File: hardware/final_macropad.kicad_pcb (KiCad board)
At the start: 4 copper layers, 91.2 x 120.5 mm, 69 parts, among them J2 2137160001, SW1 SKQGADE010, U1 ATmega32U4-A, U2 USBLC6-2SC6, U3 DM-OLED096-636, Y1 16MHz

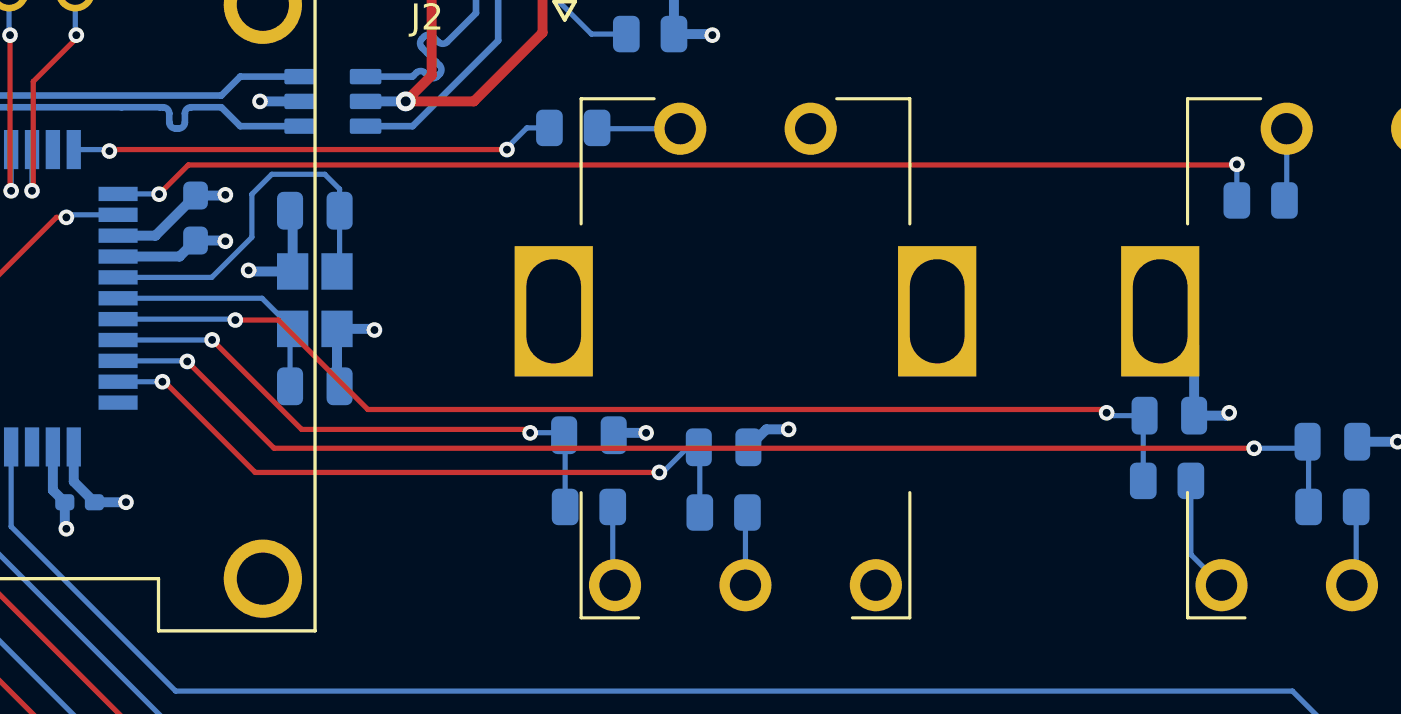
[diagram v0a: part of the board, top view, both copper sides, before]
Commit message: move trace away from through-hole
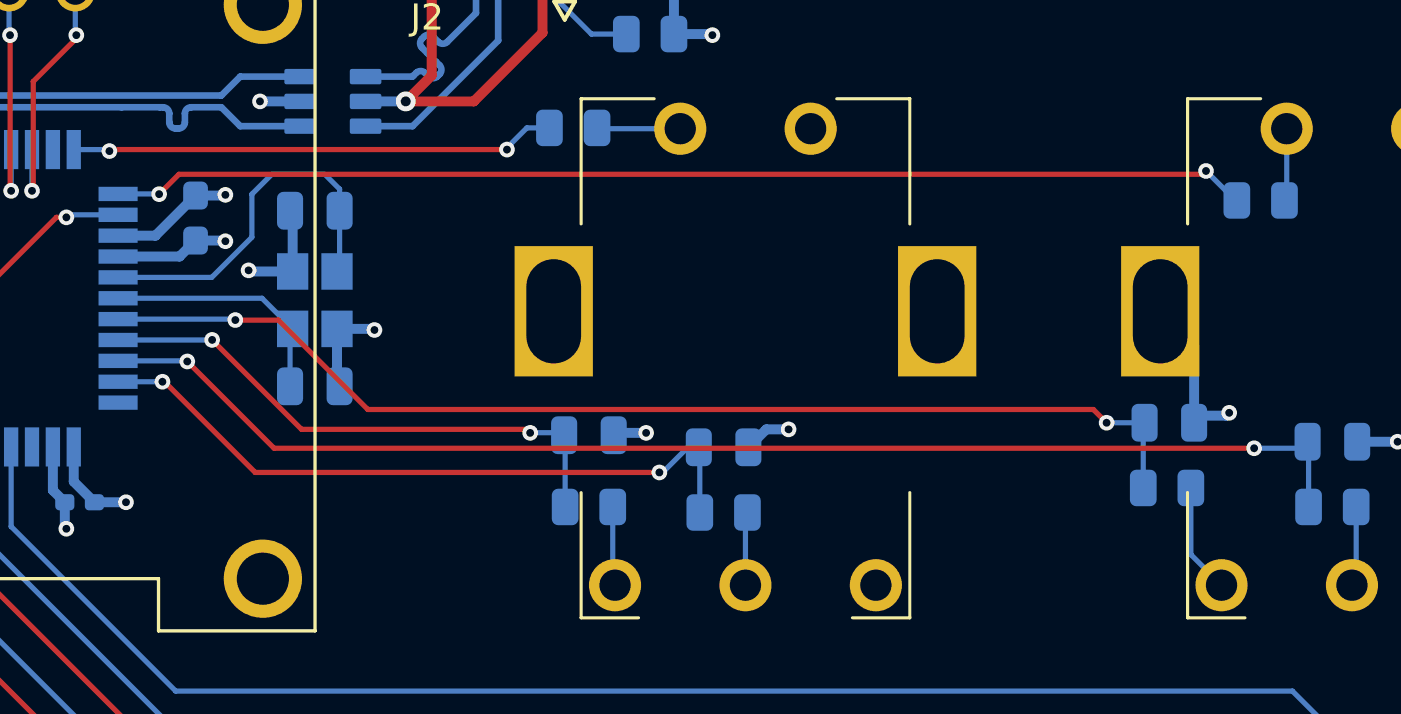
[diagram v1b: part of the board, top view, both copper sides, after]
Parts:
- moved C8 0.27 mm to (95.8, 49.0)
- moved R5 0.27 mm to (95.7, 51.5)
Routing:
- net SW0: track 44.7 -> 43.7 mm
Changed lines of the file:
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@@
 	(footprint "Resistor_SMD:R_0805_2012Metric"
 		(layer "B.Cu")
-		(at 95.6625 51.25)
+		(at 95.6625 51.522)
 		(descr "Resistor SMD 0805 (2012 Metric), square (rectangular) end terminal, IPC-7351 nominal, (Body size source: IPC-SM-782 page 72, https://www.pcb-3d.com/wordpress/wp-content/uploads/ipc-sm-782a_amendment_1_and_2.pdf), generated with kicad-footprint-generator")
 		(tags "resistor")
@@
 	(footprint "Capacitor_SMD:C_0805_2012Metric"
 		(layer "B.Cu")
-		(at 95.75 48.75)
+		(at 95.75 49.022)
 		(descr "Capacitor SMD 0805 (2012 Metric), square (rectangular) end terminal, IPC-7351 nominal, (Body size source: IPC-SM-782 page 76, https://www.pcb-3d.com/wordpress/wp-content/uploads/ipc-sm-782a_amendment_1_and_2.pdf, https://docs.google.com/spreadsheets/d/1BsfQQcO9C6DZCsRaXUlFlo91Tg2WpOkGARC1WS5S8t0/edit?usp=sharing), generated with kicad-footprint-generator")
 		(tags "capacitor")
@@
 	(segment
 		(start 97.935 48.75)
-		(end 98.044 48.641)
+		(end 96.7 48.75)
 		(width 0.381)
 		(layer "B.Cu")
@@
 	)
 	(segment
+		(start 96.7 46.05)
+		(end 95.4 44.75)
+		(width 0.381)
+		(layer "B.Cu")
+		(net 8)
+	)
+	(segment
 		(start 63.842 47.525)
 		(end 63.942 47.625)
@@
 	)
 	(segment
+		(start 96.7 48.75)
+		(end 96.7 46.05)
+		(width 0.381)
+		(layer "B.Cu")
+		(net 8)
+	)
+	(segment
 		(start 65.235 45.423)
 		(end 65.278 45.466)
@@
 	)
 	(segment
-		(start 96.7 48.75)
-		(end 97.935 48.75)
-		(width 0.381)
-		(layer "B.Cu")
-		(net 8)
-	)
-	(segment
 		(start 55.45 42.65)
 		(end 57.807 42.65)
@@
 	)
 	(segment
-		(start 62.142 40.994)
-		(end 62.042 40.894)
+		(start 98.044 48.641)
+		(end 97.935 48.75)
 		(width 0.381)
 		(layer "B.Cu")
@@
 	)
 	(segment
-		(start 96.7 48.75)
-		(end 96.7 46.05)
+		(start 62.142 40.994)
+		(end 62.042 40.894)
 		(width 0.381)
 		(layer "B.Cu")
@@
 	)
 	(segment
-		(start 96.7 46.05)
-		(end 95.4 44.75)
-		(width 0.381)
-		(layer "B.Cu")
-		(net 8)
-	)
-	(segment
 		(start 59.5365 42.037)
 		(end 59.563 42.0635)
@@
 	)
 	(segment
-		(start 98.3135 39.14)
-		(end 98.3375 39.116)
+		(start 97.028 39.497)
+		(end 57.785 39.497)
 		(width 0.2)
 		(layer "F.Cu")
@@
 	)
 	(segment
-		(start 57.023 40.259)
-		(end 58.142 39.14)
+		(start 57.785 39.497)
+		(end 57.023 40.259)
 		(width 0.2)
 		(layer "F.Cu")
@@
 	)
 	(segment
-		(start 58.142 39.14)
-		(end 98.3135 39.14)
+		(start 97.155 39.37)
+		(end 97.028 39.497)
 		(width 0.2)
 		(layer "F.Cu")
@@
 	)
 	(via
-		(at 98.3375 39.116)
+		(at 97.155 39.37)
 		(size 0.6)
 		(drill 0.3)
@@
 	)
 	(segment
-		(start 98.3375 39.116)
+		(start 98.285 40.5)
 		(end 98.3375 40.5)
 		(width 0.2)
@@
 	)
 	(segment
+		(start 97.155 39.37)
+		(end 98.285 40.5)
+		(width 0.2)
+		(layer "B.Cu")
+		(net 35)
+	)
+	(segment
 		(start 57.014 40.25)
 		(end 55.45 40.25)
@@
 	)
 	(segment
-		(start 61.595 45.085)
-		(end 59.944 45.085)
+		(start 92.837 48.514)
+		(end 65.024 48.514)
 		(width 0.2)
 		(layer "F.Cu")
@@
 	)
 	(segment
-		(start 65.024 48.514)
-		(end 61.595 45.085)
+		(start 93.345 49.022)
+		(end 92.837 48.514)
 		(width 0.2)
 		(layer "F.Cu")
@@
 	)
 	(segment
-		(start 93.218 48.514)
-		(end 65.024 48.514)
+		(start 61.595 45.085)
+		(end 59.944 45.085)
 		(width 0.2)
 		(layer "F.Cu")
@@
 	)
 	(segment
-		(start 93.345 48.641)
-		(end 93.218 48.514)
+		(start 65.024 48.514)
+		(end 61.595 45.085)
 		(width 0.2)
 		(layer "F.Cu")
@@
 	)
 	(via
-		(at 93.345 48.641)
+		(at 93.345 49.022)
 		(size 0.6)
 		(drill 0.3)
@@
 	)
 	(segment
-		(start 94.75 51.25)
-		(end 94.75 48.8)
+		(start 94.75 51.522)
+		(end 94.75 49.072)
 		(width 0.2)
 		(layer "B.Cu")
@@
 	)
 	(segment
-		(start 93.508 48.641)
-		(end 93.617 48.75)
-		(width 0.2)
-		(layer "B.Cu")
-		(net 38)
-	)
-	(segment
-		(start 93.345 48.641)
-		(end 93.508 48.641)
-		(width 0.2)
-		(layer "B.Cu")
-		(net 38)
-	)
-	(segment
-		(start 93.617 48.75)
-		(end 94.8 48.75)
+		(start 93.345 49.022)
+		(end 94.8 49.022)
 		(width 0.2)
 		(layer "B.Cu")
@@
 	)
 	(segment
-		(start 96.575 51.25)
-		(end 96.575 54.075)
+		(start 96.575 54.075)
+		(end 96.575 51.522)
 		(width 0.2)
 		(layer "B.Cu")

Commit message: build gerber files
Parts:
- added G***: LOGO, Drawings:mountainline-small, F.Cu at (49.1, 141.6)
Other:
- board text added: "MV"
- board text added: "Mini Keeb"
- board text removed: "Mini Keeb by Megan Veldhuis"
